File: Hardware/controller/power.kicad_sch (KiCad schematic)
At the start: 39 parts, among them J201 Screw_Terminal_01x03, U201 BD9D321EFJ, U202 MCP1703AT-5002E/DB, U203 ICL7660

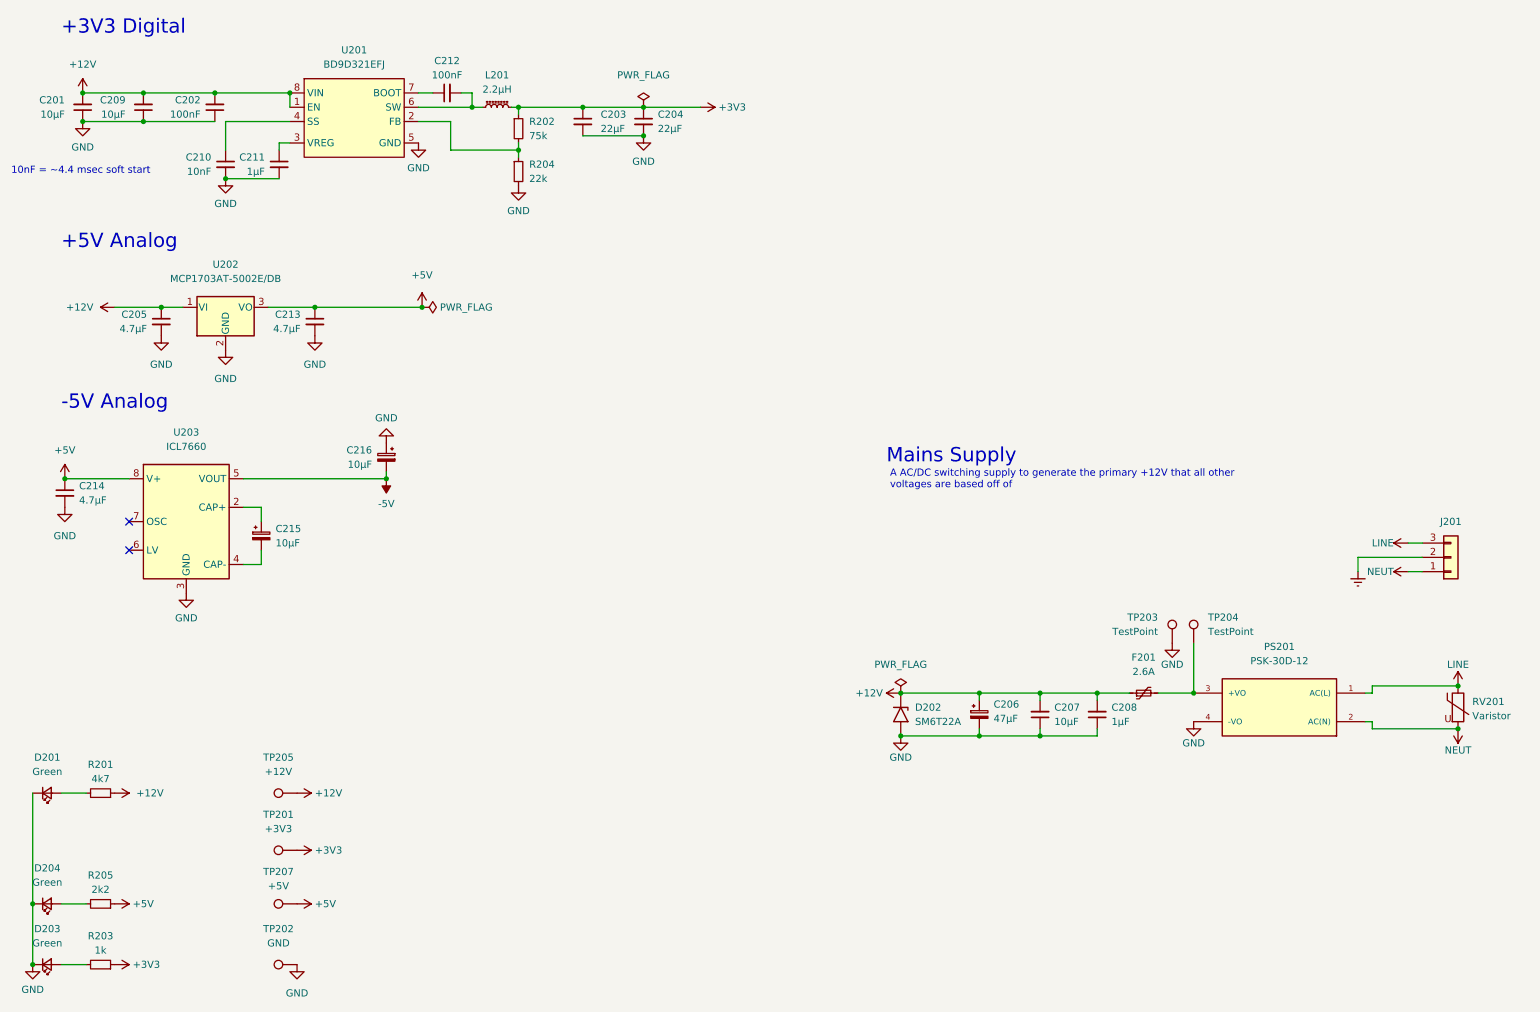
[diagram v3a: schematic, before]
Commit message: Begin cleaning up controller for rework
- Removed some of the old stuff

- Added USB host connector for front panel (including footprint for new
  ESD boi)
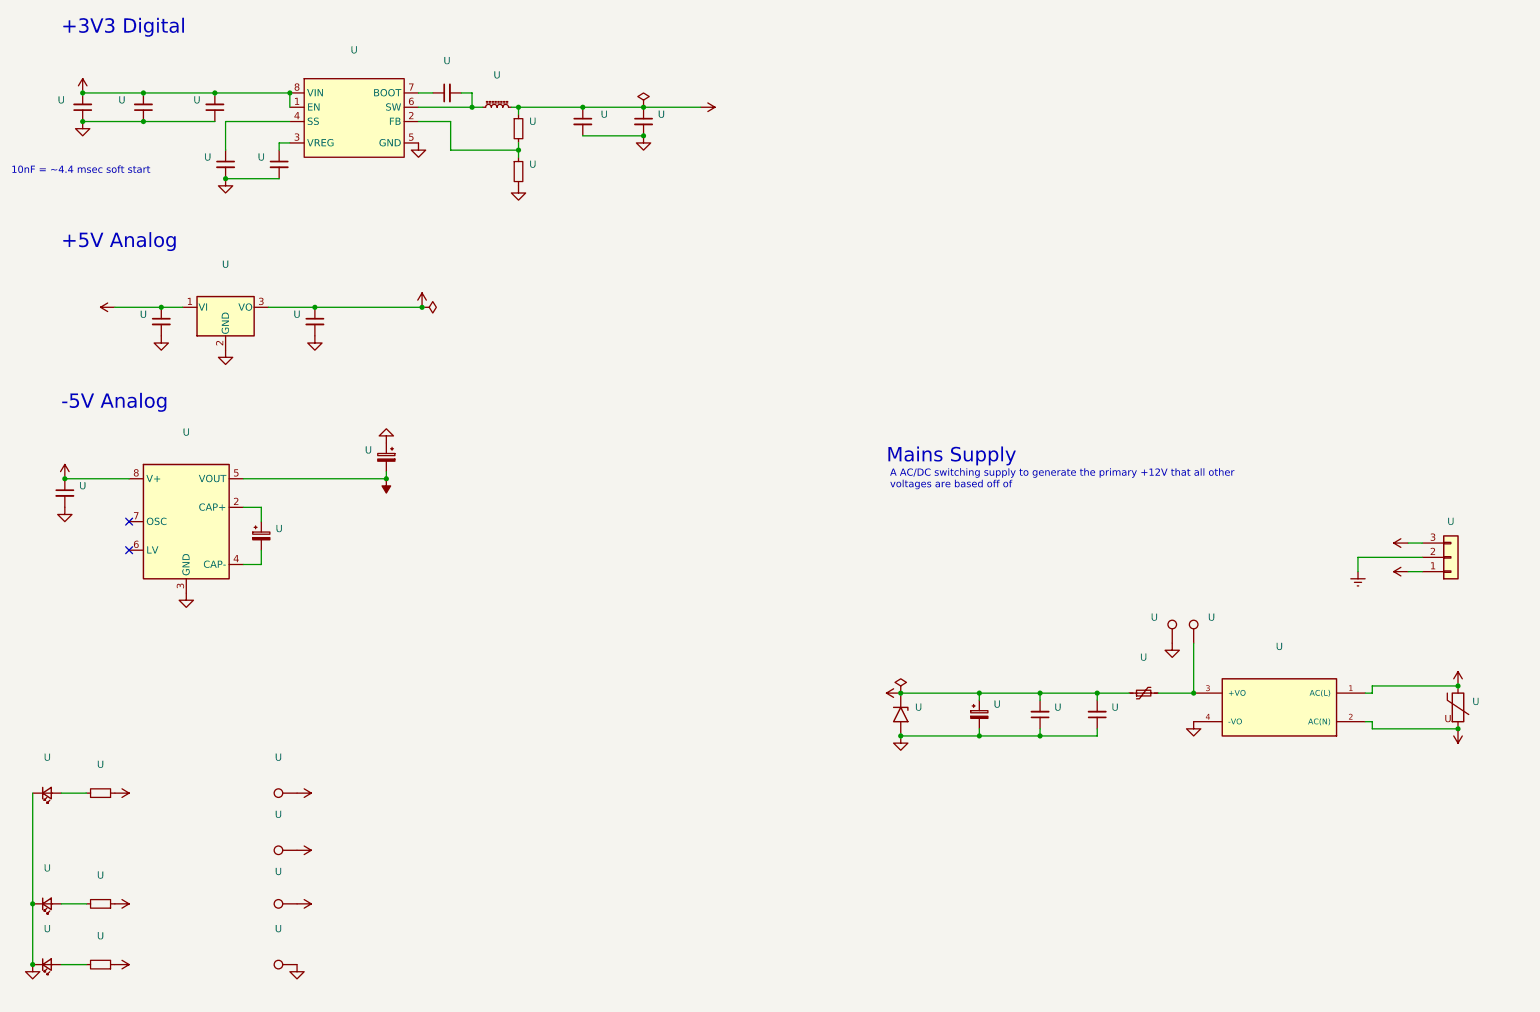
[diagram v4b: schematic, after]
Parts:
- U: renamed from PS201; value PSK-30D-12 -> (none); footprint programmable-load:CONV_PSK-30D-12 -> (none)
- U: renamed from D203; value Green -> (none); footprint LED_SMD:LED_0805_2012Metric_Pad1.15x1.40mm_HandSolder -> (none)
- U: renamed from R203; value 1k -> (none); footprint Resistor_SMD:R_0805_2012Metric_Pad1.20x1.40mm_HandSolder -> (none)
- U: renamed from C209; value 10µF -> (none); footprint Capacitor_SMD:C_0805_2012Metric_Pad1.18x1.45mm_HandSolder -> (none)
- U: renamed from TP202; value GND -> (none); footprint TestPoint:TestPoint_Keystone_5000-5004_Miniature -> (none)
- U: renamed from C202; value 100nF -> (none); footprint Capacitor_SMD:C_0805_2012Metric_Pad1.18x1.45mm_HandSolder -> (none)
- U: renamed from D202; value SM6T22A -> (none); footprint Diode_SMD:D_SMB -> (none)
- U: renamed from C212; value 100nF -> (none); footprint Capacitor_SMD:C_0805_2012Metric_Pad1.18x1.45mm_HandSolder -> (none)
- U: renamed from C201; value 10µF -> (none); footprint Capacitor_SMD:C_0805_2012Metric_Pad1.18x1.45mm_HandSolder -> (none)
- U: renamed from D204; value Green -> (none); footprint LED_SMD:LED_0805_2012Metric_Pad1.15x1.40mm_HandSolder -> (none)
- U: renamed from C214; value 4.7µF -> (none); footprint Capacitor_SMD:C_0805_2012Metric_Pad1.18x1.45mm_HandSolder -> (none)
- U: renamed from C213; value 4.7µF -> (none); footprint Capacitor_SMD:C_0805_2012Metric_Pad1.18x1.45mm_HandSolder -> (none)
- U: renamed from C204; value 22µF -> (none); footprint Capacitor_SMD:C_0805_2012Metric_Pad1.18x1.45mm_HandSolder -> (none)
- U: renamed from TP203; value TestPoint -> (none); footprint programmable-load:DELTRON-571-0x00 -> (none)
- U: renamed from D201; value Green -> (none); footprint LED_SMD:LED_0805_2012Metric_Pad1.15x1.40mm_HandSolder -> (none)
- U: renamed from U203; value ICL7660 -> (none); footprint Package_SO:SOIC-8_3.9x4.9mm_P1.27mm -> (none)
- U: renamed from C207; value 10µF -> (none); footprint Capacitor_SMD:C_0805_2012Metric_Pad1.18x1.45mm_HandSolder -> (none)
- U: renamed from TP205; value +12V -> (none); footprint TestPoint:TestPoint_Keystone_5000-5004_Miniature -> (none)
- U: renamed from C210; value 10nF -> (none); footprint Capacitor_SMD:C_0805_2012Metric_Pad1.18x1.45mm_HandSolder -> (none)
- U: renamed from C211; value 1µF -> (none); footprint Capacitor_SMD:C_0805_2012Metric_Pad1.18x1.45mm_HandSolder -> (none)
- U: renamed from TP207; value +5V -> (none); footprint TestPoint:TestPoint_Keystone_5000-5004_Miniature -> (none)
- U: renamed from TP201; value +3V3 -> (none); footprint TestPoint:TestPoint_Keystone_5000-5004_Miniature -> (none)
- U: renamed from C203; value 22µF -> (none); footprint Capacitor_SMD:C_0805_2012Metric_Pad1.18x1.45mm_HandSolder -> (none)
- U: renamed from C205; value 4.7µF -> (none); footprint Capacitor_SMD:C_0805_2012Metric_Pad1.18x1.45mm_HandSolder -> (none)
- U: renamed from R201; value 4k7 -> (none); footprint Resistor_SMD:R_0805_2012Metric_Pad1.20x1.40mm_HandSolder -> (none)
- U: renamed from R205; value 2k2 -> (none); footprint Resistor_SMD:R_0805_2012Metric_Pad1.20x1.40mm_HandSolder -> (none)
- U: renamed from R204; value 22k -> (none); footprint Resistor_SMD:R_0805_2012Metric_Pad1.20x1.40mm_HandSolder -> (none)
- U: renamed from F201; value 2.6A -> (none); footprint Fuse:Fuse_1812_4532Metric_Pad1.30x3.40mm_HandSolder -> (none)
- U: renamed from C206; value 47µF -> (none); footprint Capacitor_SMD:CP_Elec_6.3x5.4 -> (none)
- U: renamed from R202; value 75k -> (none); footprint Resistor_SMD:R_0805_2012Metric_Pad1.20x1.40mm_HandSolder -> (none)
- U: renamed from TP204; value TestPoint -> (none); footprint programmable-load:DELTRON-571-0x00 -> (none)
- U: renamed from C216; value 10µF -> (none); footprint Capacitor_Tantalum_SMD:CP_EIA-3216-18_Kemet-A_Pad1.58x1.35mm_HandSolder -> (none)
- U: renamed from U202; value MCP1703AT-5002E/DB -> (none); footprint Package_TO_SOT_SMD:SOT-223-3_TabPin2 -> (none)
- U: renamed from L201; value 2.2µH -> (none); footprint Inductor_SMD:L_Taiyo-Yuden_NR-50xx_HandSoldering -> (none)
- U: renamed from RV201; value Varistor -> (none); footprint Varistor:RV_Disc_D7mm_W3.4mm_P5mm -> (none)
- U: renamed from U201; value BD9D321EFJ -> (none); footprint Package_SO:HTSOP-8-1EP_3.9x4.9mm_P1.27mm_EP2.4x3.2mm_ThermalVias -> (none)
- U: renamed from J201; value Screw_Terminal_01x03 -> (none); footprint programmable-load:CUI_TBL002A-350-03GR-2OR -> (none)
- U: renamed from C215; value 10µF -> (none); footprint Capacitor_Tantalum_SMD:CP_EIA-3216-18_Kemet-A_Pad1.58x1.35mm_HandSolder -> (none)
- U: renamed from C208; value 1µF -> (none); footprint Capacitor_SMD:C_0805_2012Metric_Pad1.18x1.45mm_HandSolder -> (none)

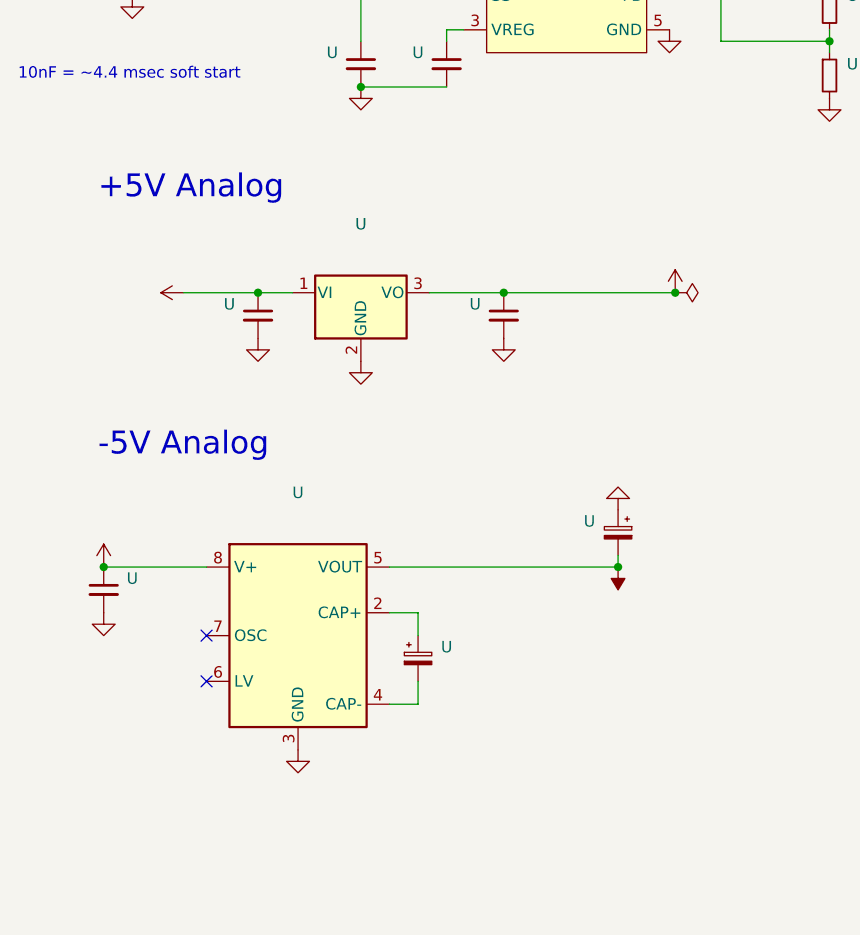
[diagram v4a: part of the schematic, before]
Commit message: More work on controller; add MYIR SoM footprint
- Begin cleaning up the controller board, that is removing all of the
  old CPU stuff and replacing it with new stuff, and general cleanup

- Create a footprint for the STM32MP1 SoM (MYR MYC-YA151C family)
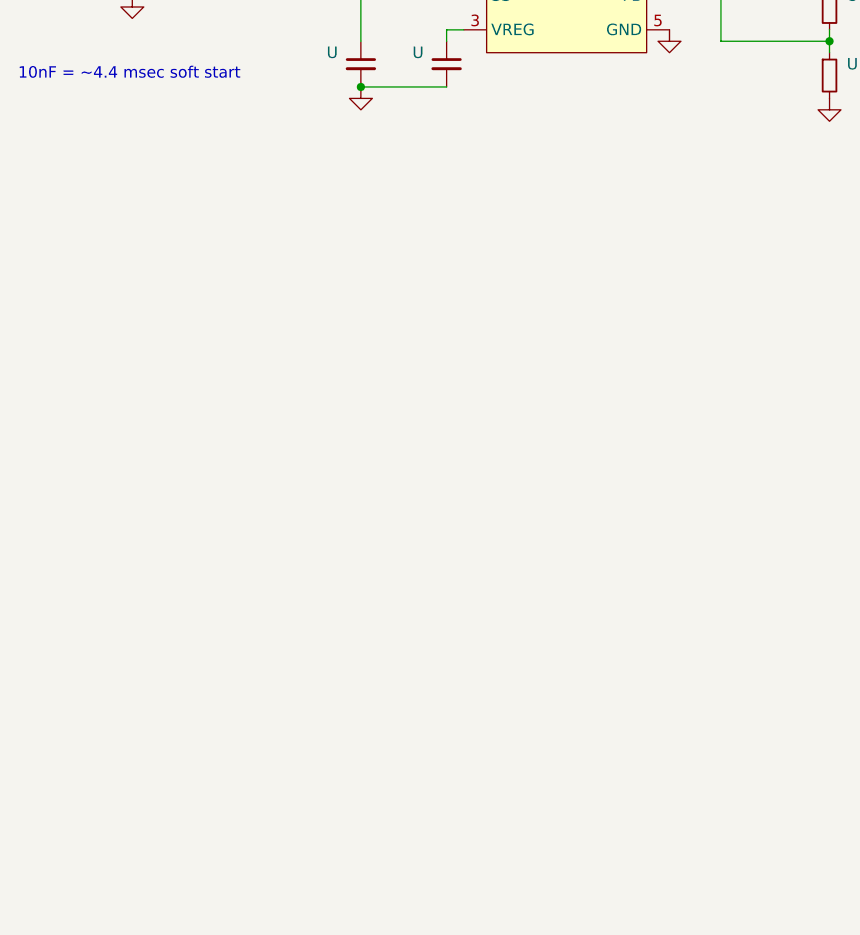
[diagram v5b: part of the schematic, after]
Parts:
- removed U (x3): (no value), symbol Device:C_Small
- removed U: (no value), symbol Regulator_SwitchedCapacitor:ICL7660
- removed U (x2): (no value), symbol Device:C_Polarized_Small
- removed U: (no value), symbol Regulator_Linear:MCP1703A-5002_SOT223
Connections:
- no-connect marks 2 -> 0
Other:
- note removed: "+5V Analog"
- note removed: "-5V Analog"
